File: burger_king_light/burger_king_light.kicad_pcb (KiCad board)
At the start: 2 copper layers, 35 x 30 mm, 1 part, among them IC1 IS32LT3177-GRLA3-TR

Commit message: wip: all ICs placed
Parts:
- added D1: MMSZ5231B-7-F, Diode_SMD:Nexperia_CFP3_SOD-123W, F.Cu at (152.7, 94.1)
- added IC2: IS32LT3178-GRLA3-TR, misc_ICs:SOIC127P600X170-9N, F.Cu at (131.6, 80.7)
- added IC3: IS32LT3178-GRLA3-TR, misc_ICs:SOIC127P600X170-9N, F.Cu at (131.6, 87.3)
- added IC4: IS32LT3178-GRLA3-TR, misc_ICs:SOIC127P600X170-9N, F.Cu at (131.6, 94.0)
- added U1: ICM7555CBAZ, Package_SO:SOIC-8_3.9x4.9mm_P1.27mm, F.Cu at (154.1, 89.2)
- IC1: value IS32LT3177-GRLA3-TR -> TPS55340PWPR; footprint misc_ICs:SOIC127P600X170-9N -> buck_boost_ICs:SOP65P640X120-15N

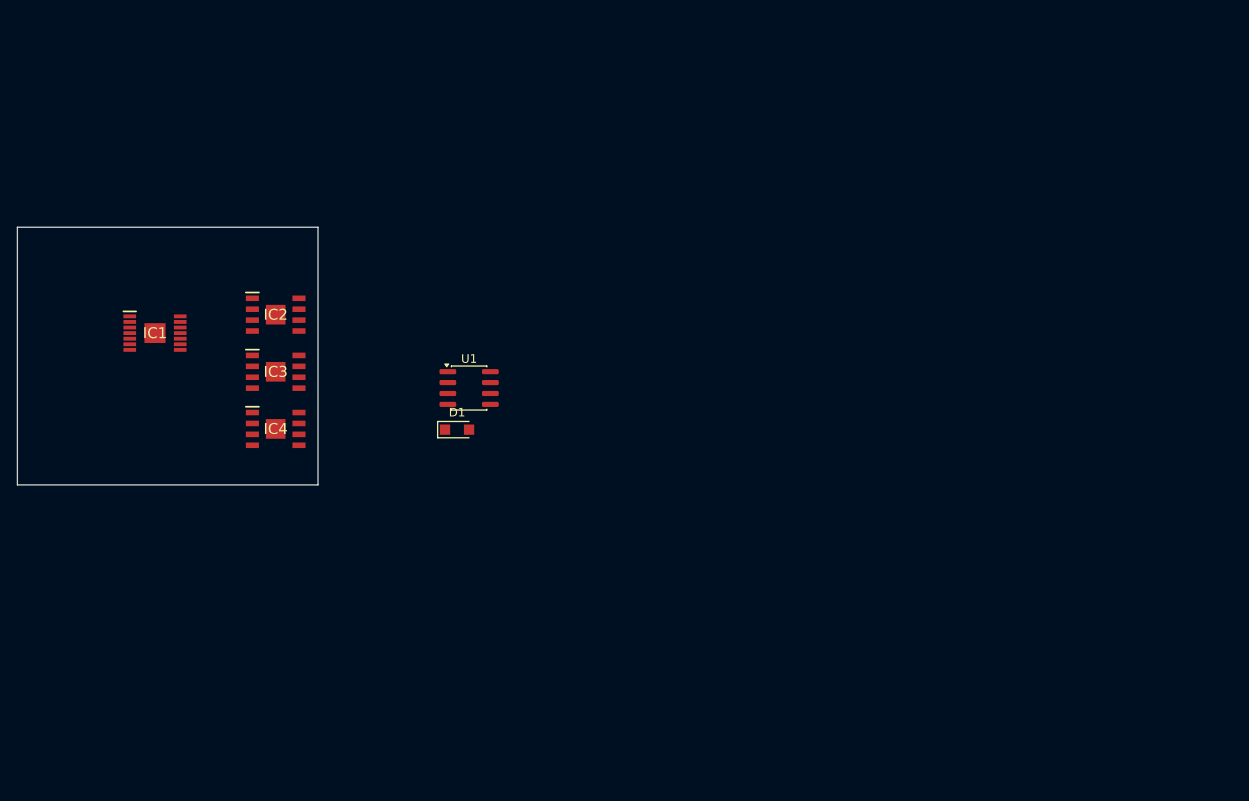
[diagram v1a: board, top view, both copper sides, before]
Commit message: laid out boost converter
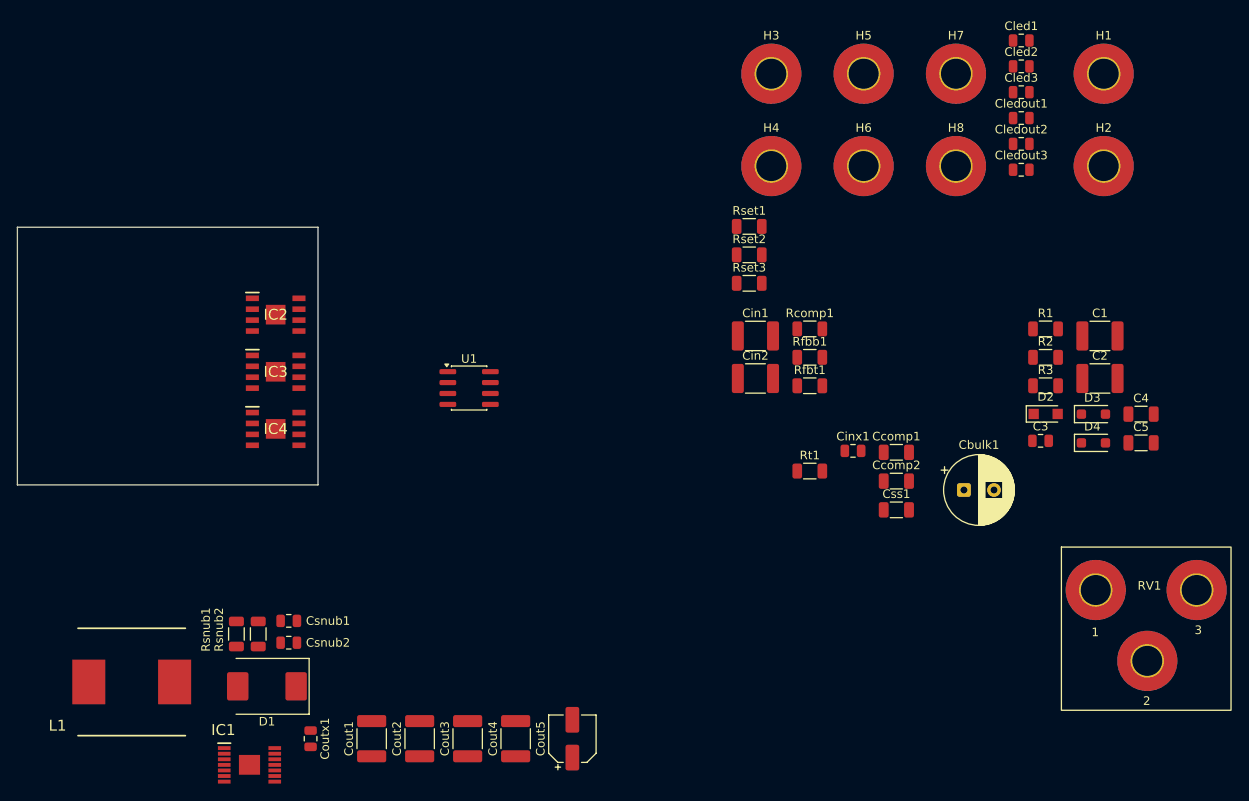
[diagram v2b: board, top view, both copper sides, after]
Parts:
- added C1: 10uF, Capacitor_SMD:C_1812_4532Metric, F.Cu at (227.5, 83.2)
- added C2: 10uF, Capacitor_SMD:C_1812_4532Metric, F.Cu at (227.5, 88.1)
- added C3: 100nF, Capacitor_SMD:C_0805_2012Metric, F.Cu at (220.6, 95.4)
- added C4: 10nF, Capacitor_SMD:C_1206_3216Metric, F.Cu at (232.3, 92.3)
- added C5: 33nF, Capacitor_SMD:C_1206_3216Metric, F.Cu at (232.3, 95.6)
- added Cbulk1: 220uF, Capacitor_THT:CP_Radial_D8.0mm_P3.50mm, F.Cu at (211.7, 101.1)
- added Ccomp1: 560pF, Capacitor_SMD:C_1206_3216Metric, F.Cu at (203.8, 96.7)
- added Ccomp2: 33nF, Capacitor_SMD:C_1206_3216Metric, F.Cu at (203.8, 100.1)
- added Cin1: 10uF, Capacitor_SMD:C_1812_4532Metric, F.Cu at (187.4, 83.2)
- added Cin2: 10uF, Capacitor_SMD:C_1812_4532Metric, F.Cu at (187.4, 88.1)
- added Cinx1: 100nF, Capacitor_SMD:C_0805_2012Metric, F.Cu at (198.8, 96.5)
- added Cled1: 100nF, Capacitor_SMD:C_0805_2012Metric, F.Cu at (218.4, 48.8)
- added Cled2: 100nF, Capacitor_SMD:C_0805_2012Metric, F.Cu at (218.4, 51.8)
- added Cled3: 100nF, Capacitor_SMD:C_0805_2012Metric, F.Cu at (218.4, 54.8)
- added Cledout1: 1nF, Capacitor_SMD:C_0805_2012Metric, F.Cu at (218.4, 57.8)
- added Cledout2: 1nF, Capacitor_SMD:C_0805_2012Metric, F.Cu at (218.4, 60.8)
- added Cledout3: 1nF, Capacitor_SMD:C_0805_2012Metric, F.Cu at (218.4, 63.8)
- added Cout1: 10uF, Capacitor_SMD:C_1812_4532Metric, F.Cu at (142.7, 130.0)
- added Cout2: 10uF, Capacitor_SMD:C_1812_4532Metric, F.Cu at (148.3, 130.0)
- added Cout3: 10uF, Capacitor_SMD:C_1812_4532Metric, F.Cu at (153.9, 130.0)
- added Cout4: 10uF, Capacitor_SMD:C_1812_4532Metric, F.Cu at (159.5, 130.0)
- added Cout5: 10uF, Capacitor_SMD:CP_Elec_5x5.3, F.Cu at (166.1, 130.0)
- added Coutx1: 2.2uF, Capacitor_SMD:C_0805_2012Metric, F.Cu at (135.6, 130.0)
- added Csnub1: 100nF, Capacitor_SMD:C_0805_2012Metric, F.Cu at (133.1, 116.3)
- added Csnub2: 100nF, Capacitor_SMD:C_0805_2012Metric, F.Cu at (133.1, 118.9)
- added Css1: 27nF, Capacitor_SMD:C_1206_3216Metric, F.Cu at (203.8, 103.4)
- added D2: 5.1V, Diode_SMD:Nexperia_CFP3_SOD-123W, F.Cu at (221.2, 92.2)
- added D3: 1N4148W, Diode_SMD:D_SOD-123F, F.Cu at (226.8, 92.3)
- added D4: 1N4148W, Diode_SMD:D_SOD-123F, F.Cu at (226.8, 95.6)
- added H1: MountingHole_Pad, MountingHole:MountingHole_3.5mm_Pad_TopBottom, F.Cu at (228.0, 52.6)
- added H2: MountingHole_Pad, MountingHole:MountingHole_3.5mm_Pad_TopBottom, F.Cu at (228.0, 63.4)
- added H3: MountingHole_Pad, MountingHole:MountingHole_3.5mm_Pad_TopBottom, F.Cu at (189.3, 52.6)
- added H4: MountingHole_Pad, MountingHole:MountingHole_3.5mm_Pad_TopBottom, F.Cu at (189.3, 63.4)
- added H5: MountingHole_Pad, MountingHole:MountingHole_3.5mm_Pad_TopBottom, F.Cu at (200.0, 52.6)
- added H6: MountingHole_Pad, MountingHole:MountingHole_3.5mm_Pad_TopBottom, F.Cu at (200.0, 63.4)
- added H7: MountingHole_Pad, MountingHole:MountingHole_3.5mm_Pad_TopBottom, F.Cu at (210.8, 52.6)
- added H8: MountingHole_Pad, MountingHole:MountingHole_3.5mm_Pad_TopBottom, F.Cu at (210.8, 63.4)
- added L1: 10uH, passives:INDPM125125X450N, F.Cu at (114.8, 123.4)
- added R1: 10, Resistor_SMD:R_1206_3216Metric, F.Cu at (221.2, 82.3)
- added R2: 560, Resistor_SMD:R_1206_3216Metric, F.Cu at (221.2, 85.6)
- added R3: 1K, Resistor_SMD:R_1206_3216Metric, F.Cu at (221.2, 89.0)
- added RV1: 100K, passives:3-PIN POT, F.Cu at (233.3, 112.7)
- added Rcomp1: 3.09K, Resistor_SMD:R_1206_3216Metric, F.Cu at (193.8, 82.3)
- added Rfbb1: 10K, Resistor_SMD:R_1206_3216Metric, F.Cu at (193.8, 85.6)
- added Rfbt1: 280K, Resistor_SMD:R_1206_3216Metric, F.Cu at (193.8, 89.0)
- added Rset1: 8.06K, Resistor_SMD:R_1206_3216Metric, F.Cu at (186.7, 70.4)
- added Rset2: 8.06K, Resistor_SMD:R_1206_3216Metric, F.Cu at (186.7, 73.7)
- added Rset3: 8.06K, Resistor_SMD:R_1206_3216Metric, F.Cu at (186.7, 77.0)
- added Rsnub1: 47.5K, Resistor_SMD:R_1206_3216Metric, F.Cu at (127.0, 117.9)
- added Rsnub2: 47.5K, Resistor_SMD:R_1206_3216Metric, F.Cu at (129.5, 117.9)
- added Rt1: 47.5K, Resistor_SMD:R_1206_3216Metric, F.Cu at (193.8, 98.9)
- D1: value MMSZ5231B-7-F -> 700 mV @ 5 A; footprint Diode_SMD:Nexperia_CFP3_SOD-123W -> Diode_SMD:D_SMC
- moved IC1 51.5 mm to (128.5, 133.1)
- moved D1 37.2 mm to (130.6, 124.0), turned to 180 degrees
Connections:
- D1 pad 1: unconnected-(D1-K-Pad1) -> +36V
- D1 pad 2: unconnected-(D1-A-Pad2) -> Net-(D1-A)
- IC1 pad 1: unconnected-(IC1-SW_1-Pad1) -> Net-(D1-A)
- IC1 pad 10: unconnected-(IC1-FREQ-Pad10) -> Net-(IC1-FREQ)
- IC1 pad 12: unconnected-(IC1-PGND_1-Pad12) -> 0
- IC1 pad 13: unconnected-(IC1-PGND_2-Pad13) -> 0
- IC1 pad 14: unconnected-(IC1-PGND_3-Pad14) -> 0
- IC1 pad 15: unconnected-(IC1-EPAD-Pad15) -> 0
- IC1 pad 2: unconnected-(IC1-SW_2-Pad2) -> Net-(D1-A)
- IC1 pad 3: unconnected-(IC1-VIN-Pad3) -> +12V
- IC1 pad 4: unconnected-(IC1-EN-Pad4) -> +12V
- IC1 pad 5: unconnected-(IC1-SS-Pad5) -> Net-(IC1-SS)
- IC1 pad 7: unconnected-(IC1-AGND-Pad7) -> 0
- IC1 pad 8: unconnected-(IC1-COMP-Pad8) -> Net-(IC1-COMP)
- IC1 pad 9: unconnected-(IC1-FB-Pad9) -> Net-(IC1-FB)
- IC2 pad 1: unconnected-(IC2-OUT_1-Pad1) -> Net-(IC2-OUT_1)
- IC2 pad 2: unconnected-(IC2-OUT_2-Pad2) -> Net-(IC2-OUT_1)
- IC2 pad 3: unconnected-(IC2-EN-Pad3) -> PWM out
- IC2 pad 4: unconnected-(IC2-ISET-Pad4) -> Net-(IC2-ISET)
- IC2 pad 5: unconnected-(IC2-GND_1-Pad5) -> 0
- IC2 pad 6: unconnected-(IC2-GND_2-Pad6) -> 0
- IC2 pad 7: unconnected-(IC2-GND_3-Pad7) -> 0
- IC2 pad 8: unconnected-(IC2-GND_4-Pad8) -> 0
- IC2 pad 9: unconnected-(IC2-GND_5-Pad9) -> 0
- IC3 pad 1: unconnected-(IC3-OUT_1-Pad1) -> Net-(IC3-OUT_1)
- IC3 pad 2: unconnected-(IC3-OUT_2-Pad2) -> Net-(IC3-OUT_1)
- IC3 pad 3: unconnected-(IC3-EN-Pad3) -> PWM out
- IC3 pad 4: unconnected-(IC3-ISET-Pad4) -> Net-(IC3-ISET)
- IC3 pad 5: unconnected-(IC3-GND_1-Pad5) -> 0
- IC3 pad 6: unconnected-(IC3-GND_2-Pad6) -> 0
- IC3 pad 7: unconnected-(IC3-GND_3-Pad7) -> 0
- IC3 pad 8: unconnected-(IC3-GND_4-Pad8) -> 0
- IC3 pad 9: unconnected-(IC3-GND_5-Pad9) -> 0
- IC4 pad 1: unconnected-(IC4-OUT_1-Pad1) -> Net-(IC4-OUT_1)
- IC4 pad 2: unconnected-(IC4-OUT_2-Pad2) -> Net-(IC4-OUT_1)
- IC4 pad 3: unconnected-(IC4-EN-Pad3) -> PWM out
- IC4 pad 4: unconnected-(IC4-ISET-Pad4) -> Net-(IC4-ISET)
- IC4 pad 5: unconnected-(IC4-GND_1-Pad5) -> 0
- IC4 pad 6: unconnected-(IC4-GND_2-Pad6) -> 0
- IC4 pad 7: unconnected-(IC4-GND_3-Pad7) -> 0
- IC4 pad 8: unconnected-(IC4-GND_4-Pad8) -> 0
- IC4 pad 9: unconnected-(IC4-GND_5-Pad9) -> 0
- U1 pad 1: unconnected-(U1-GND-Pad1) -> 0
- U1 pad 2: unconnected-(U1-TRIG-Pad2) -> Net-(U1-THRES)
- U1 pad 3: unconnected-(U1-OUT-Pad3) -> PWM out
- U1 pad 4: unconnected-(U1-~{RST}-Pad4) -> Net-(D2-K)
- U1 pad 5: unconnected-(U1-CONT-Pad5) -> Net-(U1-CONT)
- U1 pad 6: unconnected-(U1-THRES-Pad6) -> Net-(U1-THRES)
- U1 pad 8: unconnected-(U1-VCC-Pad8) -> Net-(D2-K)

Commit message: finished gridding boost circuit and LED drivers
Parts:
- removed IC1: TPS55340PWPR, buck_boost_ICs:SOP65P640X120-15N
- removed IC2, IC3, IC4: IS32LT3178-GRLA3-TR, misc_ICs:SOIC127P600X170-9N
- added U2: ICM7555CBAZ, Package_SO:SOIC-8_3.9x4.9mm_P1.27mm, F.Cu at (244.9, 136.1)
- added U3: IS32LT3178-GRLA3-TR, misc_ICs:SOIC127P600X170-9N, F.Cu at (167.6, 71.1)
- added U4: IS32LT3178-GRLA3-TR, misc_ICs:SOIC127P600X170-9N, F.Cu at (181.9, 71.1)
- added U5: IS32LT3178-GRLA3-TR, misc_ICs:SOIC127P600X170-9N, F.Cu at (196.1, 71.1)
- U1: value ICM7555CBAZ -> TPS55340PWPR; footprint Package_SO:SOIC-8_3.9x4.9mm_P1.27mm -> buck_boost_ICs:SOP65P640X120-15N
- moved H1 222.8 mm to (21.8, 137.1)
- moved H2 222.8 mm to (21.8, 147.8)
- moved Cbulk1 174.0 mm to (42.2, 140.1), turned to -90 degrees
- moved Cin2 119.8 mm to (80.3, 141.7), turned to -90 degrees
- moved Ccomp1 119.8 mm to (96.5, 149.9), turned to 180 degrees
- moved Cin1 117.3 mm to (85.9, 141.7), turned to -90 degrees
- moved Css1 115.4 mm to (96.5, 145.8), turned to 180 degrees
- moved Cinx1 112.7 mm to (95.0, 140.4), turned to -90 degrees
- moved Rcomp1 108.5 mm to (104.6, 144.3)
- moved Ccomp2 106.6 mm to (104.6, 139.2), turned to 180 degrees
- moved Rfbt1 102.6 mm to (111.3, 149.9), turned to 180 degrees
- moved Rfbb1 101.2 mm to (111.3, 144.3)
- moved Rt1 88.2 mm to (114.3, 137.2), turned to 90 degrees
- moved C1 71.7 mm to (276.9, 135.3)
- moved C2 71.7 mm to (276.9, 140.2)
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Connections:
- C4 pad 2: Net-(U1-CONT) -> Net-(U2-CONT)
- C5 pad 1: Net-(U1-THRES) -> Net-(U2-THRES)
- Ccomp1 pad 1: Net-(IC1-COMP) -> Net-(U1-COMP)
- Css1 pad 1: Net-(IC1-SS) -> Net-(U1-SS)
- R3 pad 1: Net-(U1-THRES) -> Net-(U2-THRES)
- Rcomp1 pad 1: Net-(IC1-COMP) -> Net-(U1-COMP)
- Rfbb1 pad 1: Net-(IC1-FB) -> Net-(U1-FB)
- Rfbt1 pad 2: Net-(IC1-FB) -> Net-(U1-FB)
- Rt1 pad 2: Net-(IC1-FREQ) -> Net-(U1-FREQ)
- U1 pad 1: 0 -> Net-(D1-A)
- U1 pad 2: Net-(U1-THRES) -> Net-(D1-A)
- U1 pad 3: PWM out -> +12V
- U1 pad 4: Net-(D2-K) -> +12V
- U1 pad 5: Net-(U1-CONT) -> Net-(U1-SS)
- U1 pad 6: Net-(U1-THRES) -> unconnected-(U1-SYNC-Pad6)
- U1 pad 7: unconnected-(U1-DISCH-Pad7) -> 0
- U1 pad 8: Net-(D2-K) -> Net-(U1-COMP)

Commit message: finished initial layout, created all pur regions. 4-layer design.
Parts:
- moved C4 98.8 mm to (192.9, 101.1), turned to 180 degrees
- moved D2 93.8 mm to (185.4, 104.9), turned to 180 degrees
- moved C1 93.4 mm to (192.3, 95.6)
- moved C2 93.2 mm to (188.3, 111.2), turned to -90 degrees
- moved D4 92.8 mm to (199.4, 95.5), turned to 180 degrees
- moved R2 91.5 mm to (186.9, 100.5), turned to -90 degrees
- moved R1 91.5 mm to (190.3, 90.5), turned to 90 degrees
- moved C5 90.0 mm to (199.4, 111.2)
- moved D3 89.4 mm to (199.4, 98.5)
- moved C3 86.1 mm to (192.9, 109.2)
- moved R3 78.4 mm to (199.4, 108.2)
- moved H1 71.7 mm to (74.9, 88.9)
- moved H2 71.2 mm to (74.9, 100.3)
- moved Cbulk1 63.7 mm to (85.1, 93.0)
- moved U2 60.5 mm to (192.9, 105.1), turned to 180 degrees
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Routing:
- added copper zone on F.Cu, net +12V
- added copper zone on In1.Cu, net +12V
- added copper zone on In2.Cu, net +12V
- added copper zone on F.Cu, net +36V
- added copper zone on In1.Cu, net +36V
- added copper zone on In2.Cu, net +36V
- added copper zone on B.Cu, net 0
- added copper zone on F.Cu, net 0
- added copper zone on In1.Cu, net 0
- added copper zone on In2.Cu, net 0
- added copper zone on F.Cu, net Net-(D1-A)
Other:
- board size 35 x 30 mm -> 145.3 x 49.5 mm
- copper layers 2 -> 4

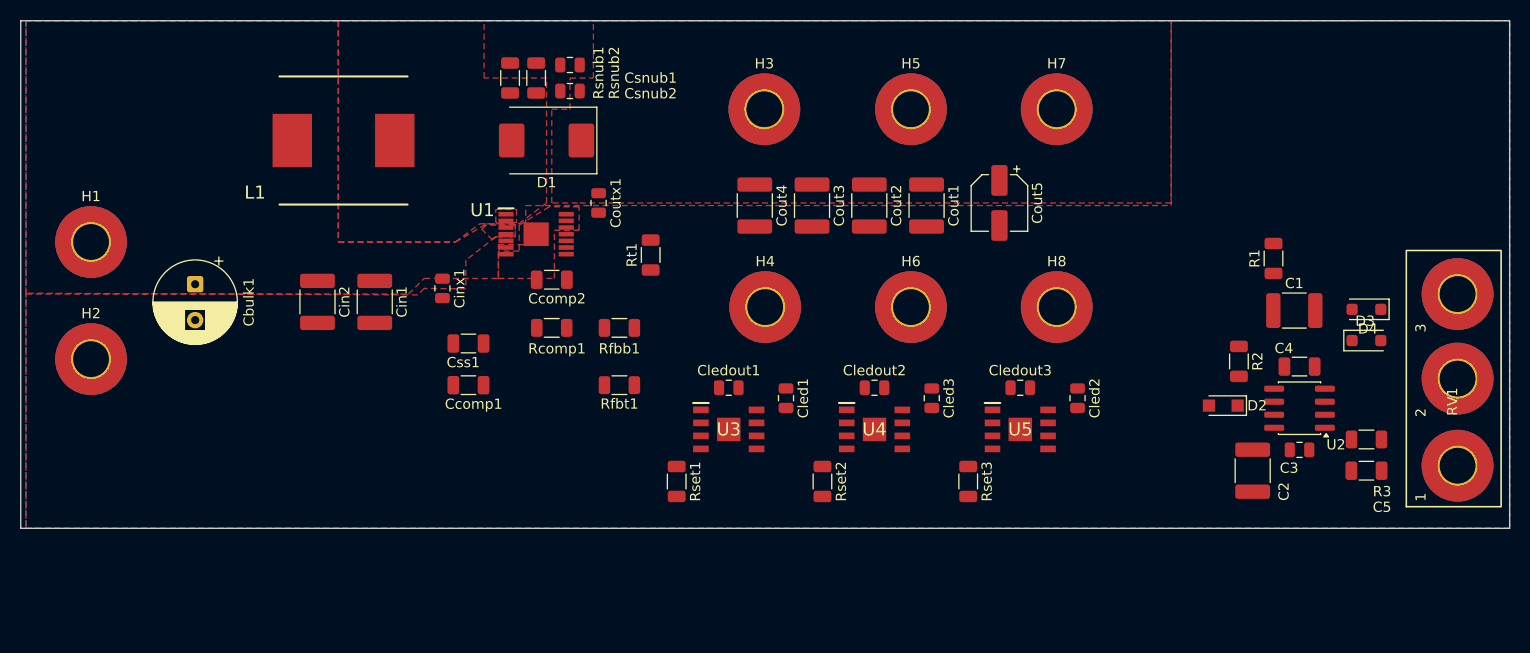
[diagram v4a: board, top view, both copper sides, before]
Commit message: finished initial routing
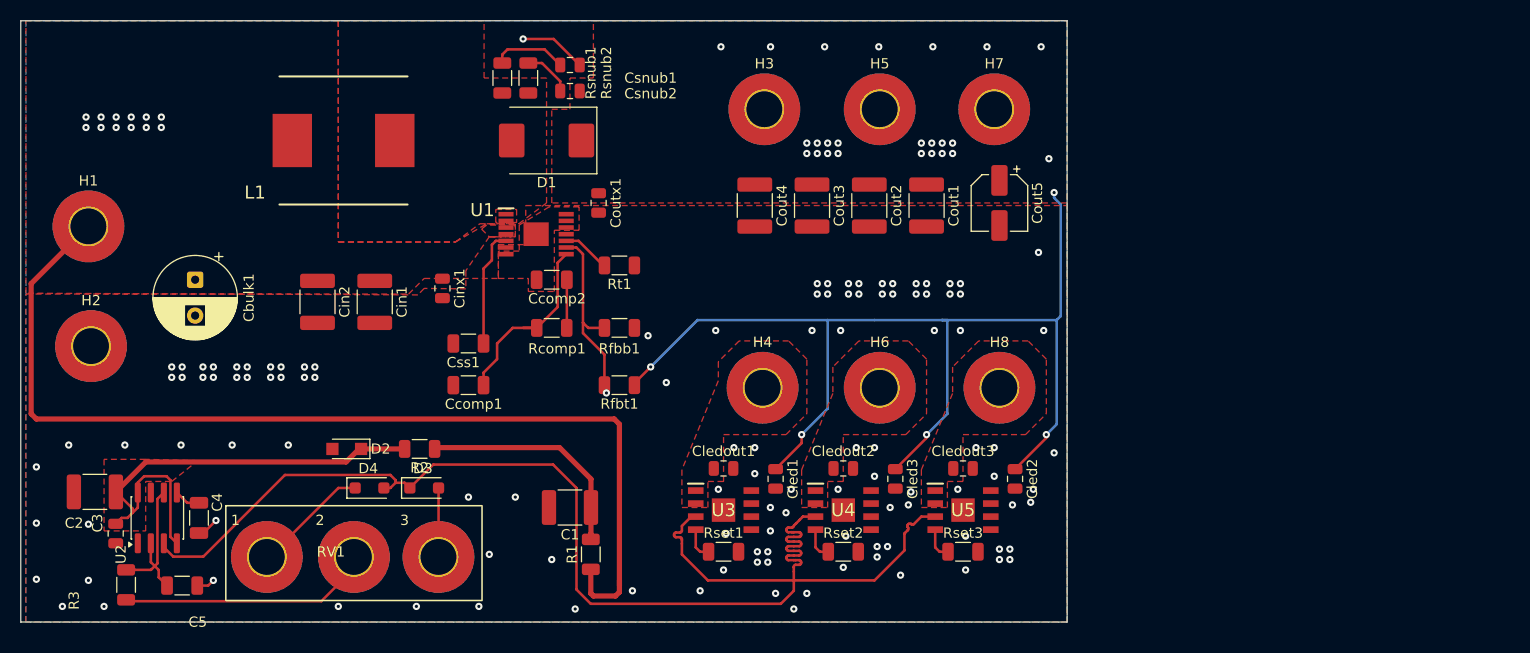
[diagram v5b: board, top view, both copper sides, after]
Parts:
- moved R3 121.9 mm to (78.4, 122.4), turned to -90 degrees
- moved C5 116.1 mm to (83.8, 122.4)
- moved C3 115.8 mm to (77.3, 117.3), turned to -90 degrees
- moved C2 113.0 mm to (75.3, 113.3), turned to 180 degrees
- moved U2 112.0 mm to (81.4, 115.8), turned to 90 degrees
- moved RV1 111.0 mm to (98.3, 119.6), turned to 0 degrees
- moved C4 108.4 mm to (85.5, 115.8), turned to 90 degrees
- moved D4 98.8 mm to (102.1, 112.9), turned to 0 degrees
- moved D3 93.1 mm to (107.4, 112.9)
- moved D2 85.6 mm to (99.9, 109.1)
- moved R2 80.4 mm to (107.0, 109.1), turned to 180 degrees
- moved C1 73.2 mm to (121.7, 114.8), turned to 180 degrees
- moved R1 72.6 mm to (123.7, 119.4)
- moved Cled2 9.96 mm to (165.1, 112.0)
- moved Cledout3 9.66 mm to (160.0, 111.0)
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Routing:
- net PWM out: track 0.00 -> 134.5 mm
- net +36V: track 0.00 -> 106.9 mm, vias 0 -> 21
- net +12V: track 0.00 -> 100.7 mm, vias 0 -> 12
- net Net-(D2-K): track 0.00 -> 47.9 mm
- net Net-(R3-Pad2): track 0.00 -> 23.6 mm
- net Net-(C1-Pad1): track 0.00 -> 22.5 mm
- net Net-(U1-COMP): track 0.00 -> 18.8 mm
- net Net-(U1-FB): track 0.00 -> 17.9 mm
- net Net-(U2-THRES): track 0.00 -> 16.2 mm
- net Net-(D4-K): track 0.00 -> 11.5 mm
- net Net-(U1-SS): track 0.00 -> 11.5 mm
- net 0: track 0.00 -> 10.5 mm, vias 0 -> 127
- net Net-(Csnub1-Pad1): track 0.00 -> 7.32 mm
- net Net-(D3-A): track 0.00 -> 6.98 mm
- net Net-(Csnub2-Pad1): track 0.00 -> 4.80 mm
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- added copper zone on F.Cu, net Net-(D2-K)
- added copper zone on F.Cu, net Net-(U3-OUT_1)
- added copper zone on F.Cu, net Net-(U4-OUT_1)
- added copper zone on F.Cu, net Net-(U5-OUT_1)
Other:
- board size 145.3 x 49.5 mm -> 102.1 x 58.7 mm
- rule pad_to_mask_clearance: 0 -> 0.0508

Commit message: working thru DRC
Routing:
- net 0: vias 127 -> 143

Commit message: finished all routing. passed DRC. ready for fab
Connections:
- U1 pad 11: unconnected-(U1-NC-Pad11) -> 0
- U1 pad 6: unconnected-(U1-SYNC-Pad6) -> 0
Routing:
- net Net-(U1-COMP): track 18.8 -> 17.5 mm
- net +36V: track 106.9 -> 105.6 mm
- net 0: track 10.5 -> 10.7 mm, vias 143 -> 152

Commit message: added better thermal coupling for led drivers. moved 12V feed circuitry for the 555. passes DRC, ready for assembly
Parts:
- moved R1 50.6 mm to (75.3, 104.6), turned to 0 degrees
- moved C1 46.8 mm to (75.3, 108.1)
- moved R2 25.9 mm to (81.2, 107.8), turned to -90 degrees
- moved D2 16.4 mm to (83.6, 107.8), turned to 90 degrees
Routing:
- net +12V: track 100.2 -> 23.1 mm
- net Net-(D2-K): track 47.9 -> 22.1 mm
- net Net-(C1-Pad1): track 22.5 -> 0.00 mm
- net PWM out: track 134.5 -> 133.1 mm
- net 0: vias 152 -> 166
- added copper zone on F.Cu, net Net-(C1-Pad1)
